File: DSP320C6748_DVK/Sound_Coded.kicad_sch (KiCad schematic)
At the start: 45 parts, among them IC16 TLV320AIC3106IRGZT, J10 SJ-3524-SMT-BE, J11 SJ-3524-SMT-BE, J12 SJ-3524-SMT-BE, Y5 ASFL1-24.576MHZ-EC-T

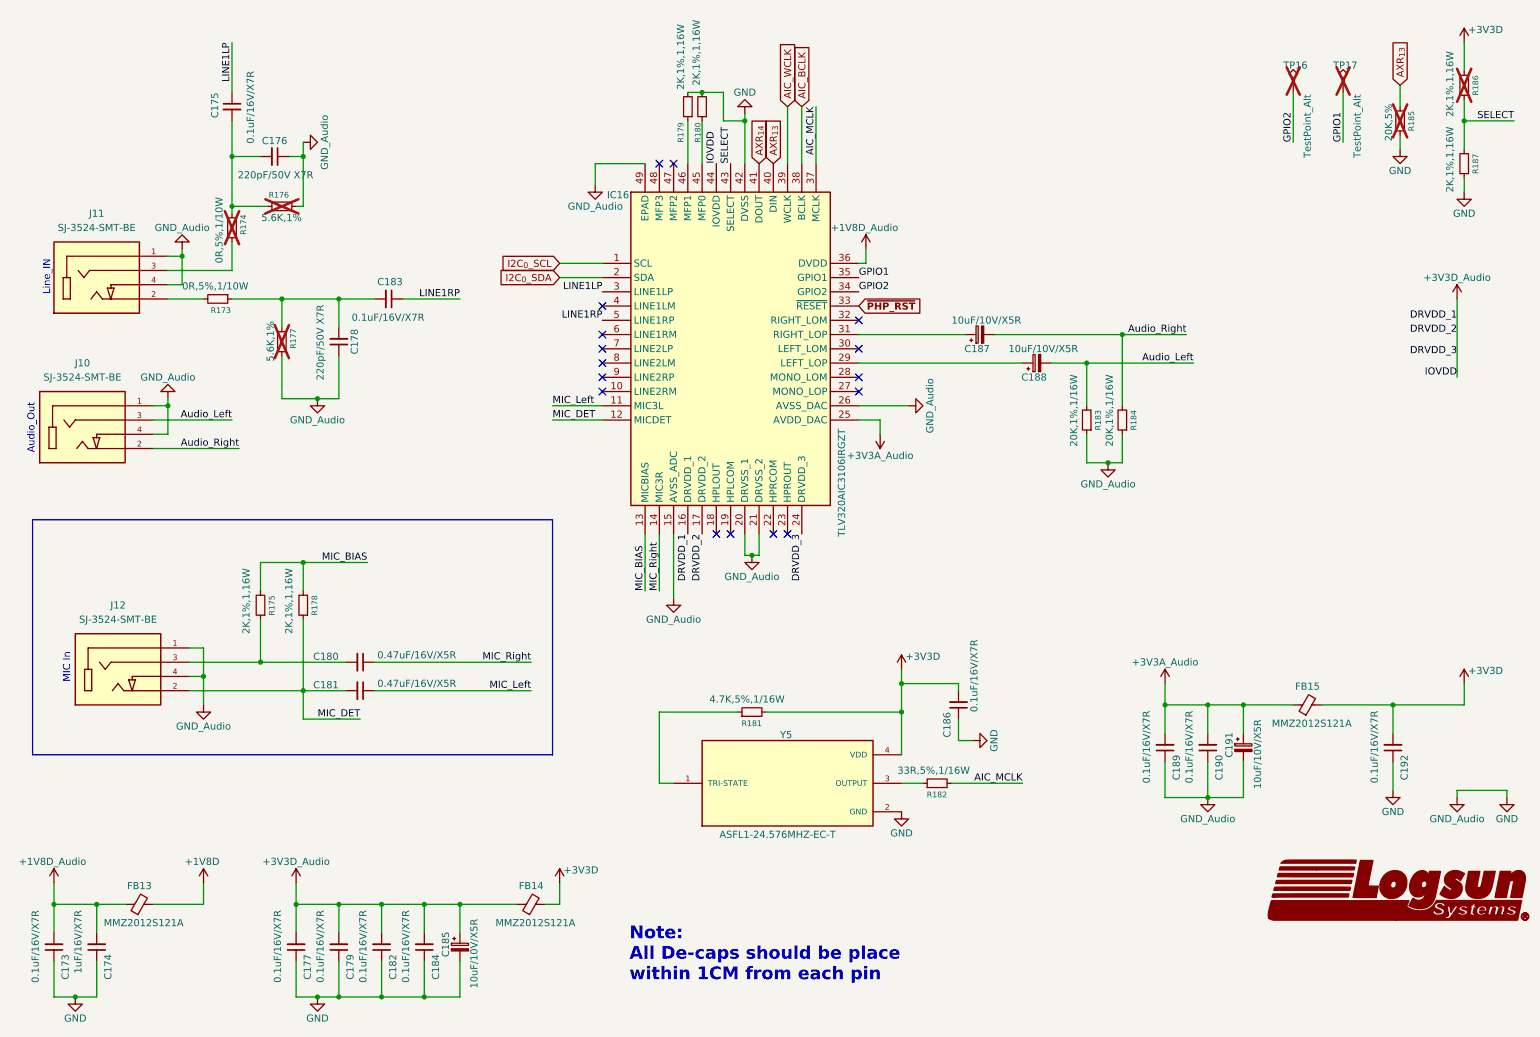
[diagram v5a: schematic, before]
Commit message: Scheamtic Re-annotation done, Some footprints assigned
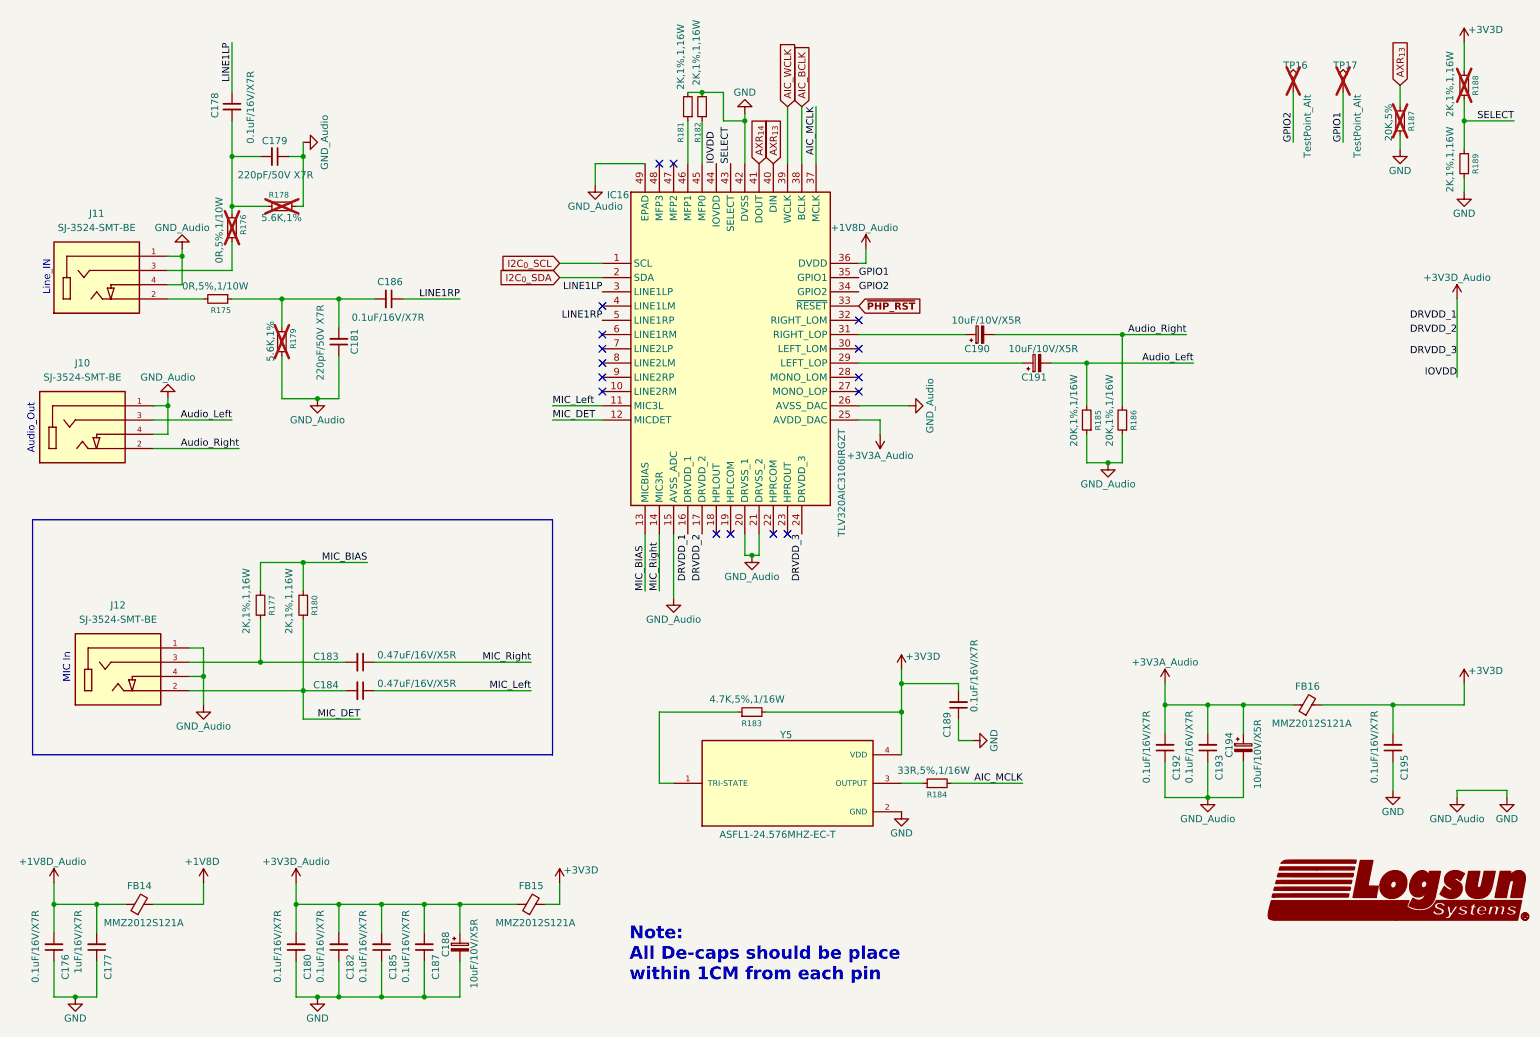
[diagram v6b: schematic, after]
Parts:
- C176: renamed from C173; footprint (none) -> Capacitor_SMD:C_0603_1608Metric_Pad1.08x0.95mm_HandSolder
- C177: renamed from C174; footprint (none) -> Capacitor_SMD:C_0603_1608Metric_Pad1.08x0.95mm_HandSolder
- C178: renamed from C175; footprint (none) -> Capacitor_SMD:C_0603_1608Metric_Pad1.08x0.95mm_HandSolder
- C179: renamed from C176; footprint (none) -> Capacitor_SMD:C_0603_1608Metric_Pad1.08x0.95mm_HandSolder
- C180: renamed from C177; footprint (none) -> Capacitor_SMD:C_0603_1608Metric_Pad1.08x0.95mm_HandSolder
- C181: renamed from C178; footprint (none) -> Capacitor_SMD:C_0603_1608Metric_Pad1.08x0.95mm_HandSolder
- C182: renamed from C179; footprint (none) -> Capacitor_SMD:C_0603_1608Metric_Pad1.08x0.95mm_HandSolder
- C183: renamed from C180; footprint (none) -> Capacitor_SMD:C_0603_1608Metric_Pad1.08x0.95mm_HandSolder
- C184: renamed from C181; footprint (none) -> Capacitor_SMD:C_0603_1608Metric_Pad1.08x0.95mm_HandSolder
- C185: renamed from C182; footprint (none) -> Capacitor_SMD:C_0603_1608Metric_Pad1.08x0.95mm_HandSolder
- C186: renamed from C183; footprint (none) -> Capacitor_SMD:C_0603_1608Metric_Pad1.08x0.95mm_HandSolder
- C187: renamed from C184; footprint (none) -> Capacitor_SMD:C_0603_1608Metric_Pad1.08x0.95mm_HandSolder
- C188: renamed from C185; footprint (none) -> Capacitor_SMD:C_0603_1608Metric_Pad1.08x0.95mm_HandSolder
- C189: renamed from C186; footprint (none) -> Capacitor_SMD:C_0603_1608Metric_Pad1.08x0.95mm_HandSolder
- C190: renamed from C187; footprint (none) -> Capacitor_SMD:C_0603_1608Metric_Pad1.08x0.95mm_HandSolder
- C191: renamed from C188; footprint (none) -> Capacitor_SMD:C_0603_1608Metric_Pad1.08x0.95mm_HandSolder
- C192: renamed from C189; footprint (none) -> Capacitor_SMD:C_0603_1608Metric_Pad1.08x0.95mm_HandSolder
- C193: renamed from C190; footprint (none) -> Capacitor_SMD:C_0603_1608Metric_Pad1.08x0.95mm_HandSolder
- C194: renamed from C191; footprint (none) -> Capacitor_SMD:C_0603_1608Metric_Pad1.08x0.95mm_HandSolder
- C195: renamed from C192; footprint (none) -> Capacitor_SMD:C_0603_1608Metric_Pad1.08x0.95mm_HandSolder
- FB14: renamed from FB13; footprint (none) -> Inductor_SMD:L_0805_2012Metric_Pad1.05x1.20mm_HandSolder
- FB15: renamed from FB14; footprint (none) -> Inductor_SMD:L_0805_2012Metric_Pad1.05x1.20mm_HandSolder
- FB16: renamed from FB15; footprint (none) -> Inductor_SMD:L_0805_2012Metric_Pad1.05x1.20mm_HandSolder
- R175: renamed from R173; footprint (none) -> Resistor_SMD:R_0603_1608Metric_Pad0.98x0.95mm_HandSolder
- R176: renamed from R174; footprint (none) -> Resistor_SMD:R_0603_1608Metric_Pad0.98x0.95mm_HandSolder
- R177: renamed from R175; footprint (none) -> Resistor_SMD:R_0603_1608Metric_Pad0.98x0.95mm_HandSolder
- R178: renamed from R176; footprint (none) -> Resistor_SMD:R_0603_1608Metric_Pad0.98x0.95mm_HandSolder
- R179: renamed from R177; footprint (none) -> Resistor_SMD:R_0603_1608Metric_Pad0.98x0.95mm_HandSolder
- R180: renamed from R178; footprint (none) -> Resistor_SMD:R_0603_1608Metric_Pad0.98x0.95mm_HandSolder
- R181: renamed from R179; footprint (none) -> Resistor_SMD:R_0603_1608Metric_Pad0.98x0.95mm_HandSolder
- R182: renamed from R180; footprint (none) -> Resistor_SMD:R_0603_1608Metric_Pad0.98x0.95mm_HandSolder
- R183: renamed from R181; footprint (none) -> Resistor_SMD:R_0603_1608Metric_Pad0.98x0.95mm_HandSolder
- R184: renamed from R182; footprint (none) -> Resistor_SMD:R_0603_1608Metric_Pad0.98x0.95mm_HandSolder
- R185: renamed from R183; footprint (none) -> Resistor_SMD:R_0603_1608Metric_Pad0.98x0.95mm_HandSolder
- R186: renamed from R184; footprint (none) -> Resistor_SMD:R_0603_1608Metric_Pad0.98x0.95mm_HandSolder
- R187: renamed from R185; footprint (none) -> Resistor_SMD:R_0603_1608Metric_Pad0.98x0.95mm_HandSolder
- R188: renamed from R186; footprint (none) -> Resistor_SMD:R_0603_1608Metric_Pad0.98x0.95mm_HandSolder
- R189: renamed from R187; footprint (none) -> Resistor_SMD:R_0603_1608Metric_Pad0.98x0.95mm_HandSolder
- TP16, TP17: footprint (none) -> TestPoint:TestPoint_Pad_D3.0mm
